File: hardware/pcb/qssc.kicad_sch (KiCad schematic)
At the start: 80 parts, among them J1 FT232RL, J10 USB-C, J11 Samtec LSHM-130, J2 5V Barrel, J3 SMA, J7 RESET, J8 MW_GATE, J9 JTAG, U1 XC7A35T-1CPG236C, U3 ADF4351BCPZ, U5 HMC441LP3E, U8 W25Q128JVSIQ, Y1 100MHz TCXO

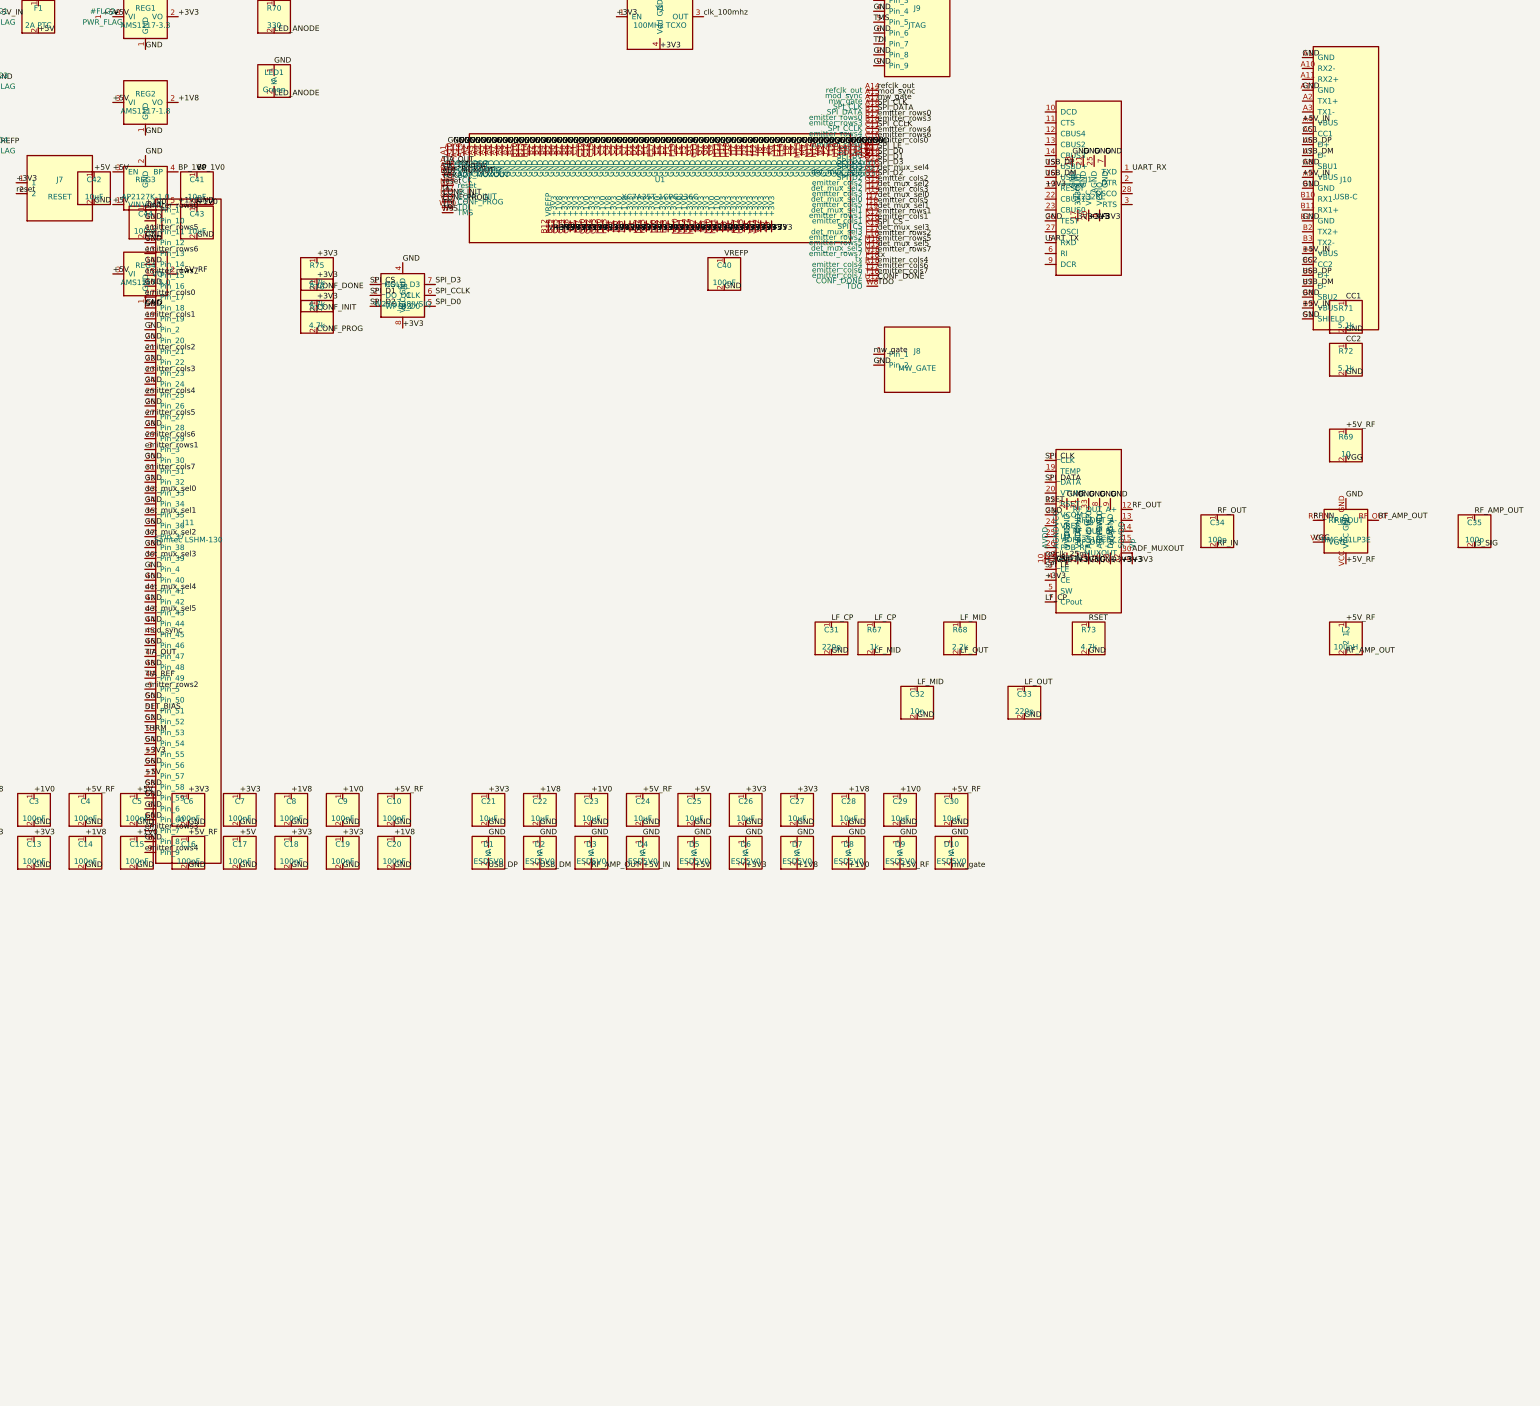
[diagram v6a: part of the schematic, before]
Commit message: pcb: fix router keepout bugs -> both boards DRC-clean (0/0/0)
The headless line router had three keepout bugs that let a via or track
claim a cell another net already owned, producing DRC shorts on the
production-hardened (denser) board:

1. Centre-only via check. _via_candidates / _bga_edge_via_candidates /
   _via_point_clear only tested the via's centre cell per layer, but
   _add_via then marked a full r3 (0.6 mm) block on all four signal
   layers. A neighbour net's track 0.1-0.6 mm off-centre was invisible,
   so the via was placed and shorted it (CONF_DONE via vs CONF_INIT
   track on In4.Cu; TIA_ADC via vs VREFP track on B.Cu). Fixed with a
   _via_footprint_free helper that checks the full r3 footprint on all
   four signal layers before accepting any via-up.

2. multi_vip (BGA via-in-pad). The per-net vip_net "allowed" override
   seeded each ball's r2 mark on In3/In4/B.Cu. Adjacent 0.5 mm-pitch
   balls' r2 marks overlap by 0.3 mm, and the override let a net's own
   track/via-up enter that overlap -> ~0.10 mm clearance to the
   neighbour VIP. The multi_keepout fix (for pads) did not cover VIPs.
   Fixed by building a multi_vip set (cells in >=2 nets' VIP marks) and
   subtracting it from every net's vip_net, mirroring multi_keepout.

3. multi_keepout (pads) -- already applied last session (mw_gate->GND
   short on the D10 ESD diode). Kept; documented alongside multi_vip.

Result: both boards regenerate + route DRC-clean headlessly:
  qssc:        14/71 non-plane nets, 217 tracks, 95 vias, 0 DRC violations
  chip_module: 11/133 nets, 140 tracks, 47 vias, 0 DRC violations
ERC: 0 errors on both schematics (warnings only).

The router is now provably no-short-by-construction, but the correct
keepouts are conservative (a THROUGH via-up needs its full 0.6 mm
footprint clear on all four signal layers, which the dense 0.5 mm BGA
escape rarely affords), so completeness dropped from a buggy 37 (centre-
only check placed shorting vias) to a correct 14. The headles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
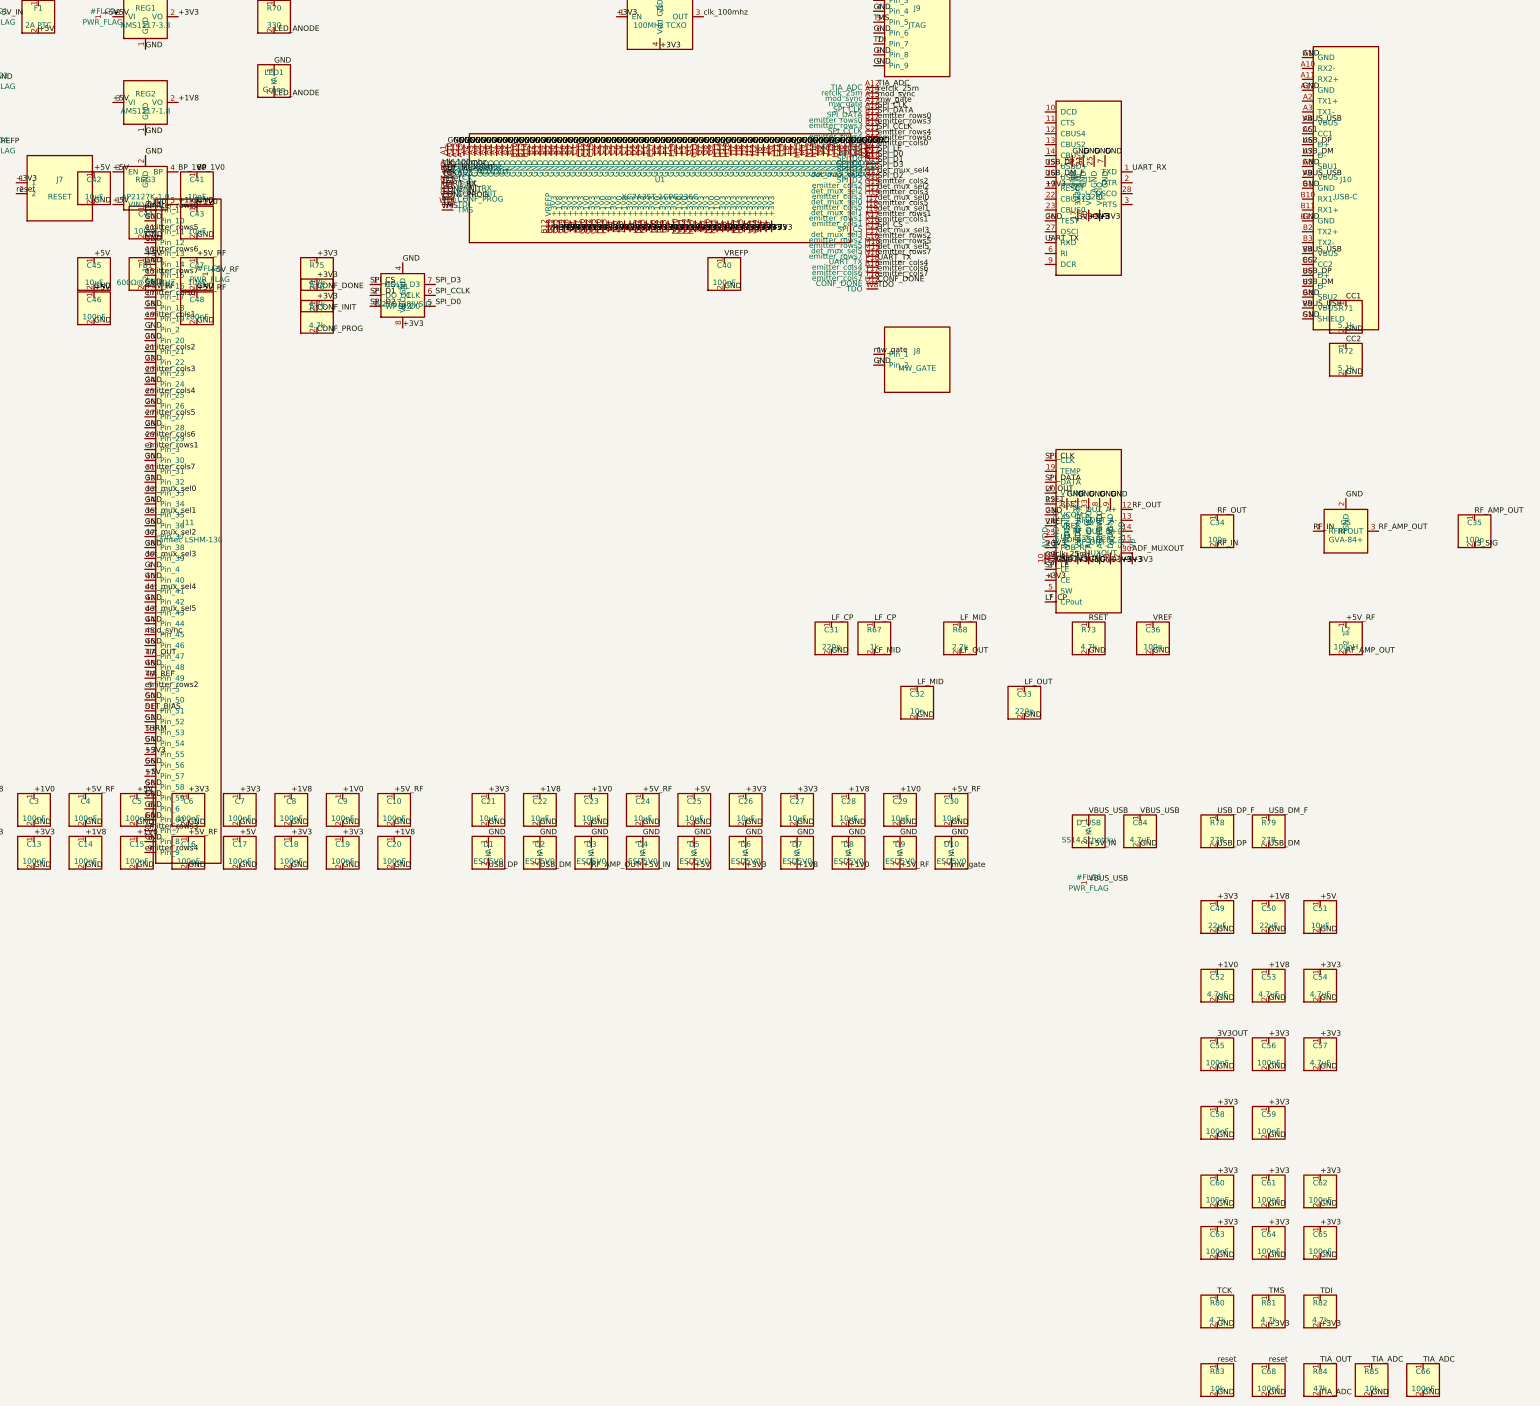
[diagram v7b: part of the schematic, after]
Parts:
- removed R69: 10, Resistor_SMD:R_0805_2012Metric, symbol qssc:R
- removed REG4: AMS1117-5.0, Package_TO_SOT_SMD:SOT-223-3_TabPin2, symbol qssc:AMS1117-5.0
- removed U5: HMC441LP3E, Package_DFN_QFN:QFN-16-1EP_3x3mm_P0.5mm_EP1.45x1.45mm, symbol qssc:HMC441LP3E
- added C36: 100n, Capacitor_SMD:C_0603_1608Metric, symbol qssc:C
- added C45, C47, C51: 10uF, Capacitor_SMD:C_0805_2012Metric, symbol qssc:C
- added C46, C48, C55, C56, C58, C59, C60, C61, C62, C63, C64, C65, C66, C68: 100nF, Capacitor_SMD:C_0603_1608Metric, symbol qssc:C
- added C49, C50: 22uF, Capacitor_SMD:C_0805_2012Metric, symbol qssc:C
- added C52, C53, C54, C57, C84: 4.7uF, Capacitor_SMD:C_0805_2012Metric, symbol qssc:C
- added D_USB: SS14 Schottky, Diode_SMD:D_SMA, symbol qssc:D
- added FB1: 600Ω@100MHz, Inductor_SMD:L_0603_1608Metric, symbol qssc:L
- added R78, R79: 27R, Resistor_SMD:R_0603_1608Metric, symbol qssc:R
- added R80, R81, R82: 4.7k, Resistor_SMD:R_0603_1608Metric, symbol qssc:R
- added R83, R85: 10k, Resistor_SMD:R_0603_1608Metric, symbol qssc:R
- added R84: 47k, Resistor_SMD:R_0603_1608Metric, symbol qssc:R
- added U5: GVA-84+, Package_TO_SOT_SMD:SOT-89-3, symbol qssc:GVA-84
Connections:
- net refclk_out is gone; now on net refclk_25m: U1.A14 (refclk_25m)
- net rx is gone; now on net UART_RX: U1.P17 (UART_RX)
- net tx is gone; now on net UART_TX: U1.P18 (UART_TX)
- net +1V0: now also C52.1
- net +1V8: now also C50.1, C53.1
- net +3V3: now also U3.26 (PDB_RF), C49.1, C54.1, C56.1, C57.1, C58.1, C59.1, C60.1, C61.1, C62.1, C63.1, C64.1, C65.1, R81.2, R82.2
- net +5V: now also C45.1, C46.1, C51.1, FB1.1
- net +5V_IN: now also D_USB.2 (A); no longer J10.A4 (VBUS), J10.A9 (VBUS), J10.B4 (VBUS), J10.B9 (VBUS)
- net +5V_RF: now also C47.1, C48.1, FB1.2
- net 3V3OUT: now also C55.1
- net GND: now also C36.2, C45.2, C46.2, C47.2, C48.2, C49.2, C50.2, C51.2, C52.2, C53.2, C54.2, C55.2, C56.2, C57.2, C58.2, C59.2, C60.2, C61.2, C62.2, C63.2, C64.2, C65.2, C66.2, C68.2, C84.2, R80.2, R83.2, R85.2, U5.2 (GND)
- net LF_OUT: now also U3.20 (VTUNE)
- net RF_AMP_OUT: now also U5.3 (RFOUT)
- net RF_IN: now also U5.1 (RFIN)
- net TCK: now also R80.1
- net TDI: now also R82.1
- net TIA_OUT: now also R84.1; no longer U1.A12 (TIA_OUT)
- net TMS: now also R81.1
- net USB_DM: now also R79.2; no longer J1.16 (USBD-)
- net USB_DP: now also R78.2; no longer J1.15 (USBD+)
- net reset: now also C68.1, R83.1
- net VREF: now reaches U3.24 (VREF)
- net VREF: now also C36.1
- new net TIA_ADC: C66.1, R84.2, R85.1, U1.A12 (TIA_ADC)
- new net USB_DM_F: J1.16 (USBD-), R79.1
- new net USB_DP_F: J1.15 (USBD+), R78.1
- new net VBUS_USB: C84.1, D_USB.1 (K), J10.A4 (VBUS), J10.A9 (VBUS), J10.B4 (VBUS), J10.B9 (VBUS)
